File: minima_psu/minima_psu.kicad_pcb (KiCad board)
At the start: 2 copper layers, 78 x 90 mm, 26 parts, among them J1 Screw_Terminal_01x03, J2 Screw_Terminal_01x02, J3 Screw_Terminal_01x03, J4 Screw_Terminal_01x03, J5 Screw_Terminal_01x03, J6 Screw_Terminal_01x03

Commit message: Minor PCB adjustements
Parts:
- moved C4 15.4 mm to (104.2, 126.8), turned to 270 degrees
- moved C6 13.8 mm to (138.2, 141.8)
- moved C7 10.9 mm to (126.2, 126.8)
- moved J2 9.00 mm to (136.2, 151.8)
- moved J4 9.00 mm to (148.2, 151.8)
- moved J5 2.83 mm to (158.2, 75.8)
- moved R4 2.54 mm to (101.6, 116.8)
- moved J1 2.24 mm to (120.2, 75.8)
- moved J6 2.24 mm to (142.2, 75.8)
- moved D1 2.00 mm to (148.2, 141.8)
- moved C2 1.27 mm to (101.6, 97.8)
- moved C3 1.27 mm to (111.8, 97.8)
- moved R3 1.27 mm to (101.6, 105.4)
- moved R5 1.27 mm to (101.6, 113.0)
- moved C9 1.21 mm to (153.7, 97.8)
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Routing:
- net /ac_l: track 0.00 -> 102.3 mm
- net Earth_Protective: track 0.00 -> 65.7 mm
- net /ac_n: track 0.00 -> 39.6 mm
- net Net-(C6-Pad1): track 0.00 -> 38.6 mm
- net Net-(C2-Pad1): track 0.00 -> 17.5 mm
- net Net-(C3-Pad2): track 0.00 -> 13.2 mm
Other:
- net class ac_p added: clearance 2, trace_width 2.54, via_dia 0.8, via_drill 0.4
- net class ac_prot added: clearance 2, trace_width 5.08, via_dia 0.8, via_drill 0.4
- net class dc_p added: clearance 1, trace_width 5.08, via_dia 0.8, via_drill 0.4

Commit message: WIP: Layout of PCB.
Signed-off-by: Nenad Radulovic <nenad.b.radulovic@gmail.com>
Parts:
- added LOGO1: Kicad_Logo, Symbol:KiCad-Logo_5mm_Copper, F.Cu at (145.2, 86.8)
- added LOGO2: Kicad_Logo, Symbol:OSHW-Logo2_7.3x6mm_SilkScreen, F.Cu at (168.2, 84.8)
- moved C2 14.9 mm to (114.2, 89.8), turned to 180 degrees
- moved R2 13.2 mm to (106.2, 96.8)
- moved D2 11.3 mm to (100.2, 98.8), turned to 270 degrees
- moved R4 11.0 mm to (106.2, 106.8)
- moved C3 10.3 mm to (105.2, 89.8), turned to 180 degrees
- moved R3 5.86 mm to (106.2, 101.8)
- moved R5 4.80 mm to (106.2, 111.8)
- moved C8 2.06 mm to (127.0, 99.8)
- moved C9 2.06 mm to (153.7, 99.8)
- moved J1 2.00 mm to (120.2, 77.8)
- moved J5 2.00 mm to (158.2, 77.8)
- moved J6 2.00 mm to (142.2, 77.8)
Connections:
- net Net-(C2-Pad1) renamed /acs_p
- net Net-(C3-Pad2) renamed /acs_n
- R3 pad 1: GNDPWR -> Net-(C3-Pad1)
- R3 pad 2: Net-(C3-Pad1) -> GNDPWR
- R5 pad 1: GNDPWR -> /vee
- R5 pad 2: /vee -> GNDPWR
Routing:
- net /acs_p: track 17.5 -> 0.00 mm
- net Net-(C3-Pad1): track 0.00 -> 14.1 mm
- net /acs_n: track 13.2 -> 0.00 mm
- net Net-(C2-Pad2): track 0.00 -> 8.24 mm
- added copper zone on B.Cu, net /acs_n
- added copper zone on B.Cu, net /acs_p

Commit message: WIP: Component routing & placement
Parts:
- removed the J4 at (148.2, 151.8)
- added C3: 100n, Capacitor_THT:C_Rect_L7.0mm_W3.5mm_P5.00mm, F.Cu at (130.8, 85.7)
- added C4: 100n, Capacitor_THT:C_Rect_L7.0mm_W3.5mm_P5.00mm, F.Cu at (148.0, 85.7)
- added C7: 100n, Capacitor_THT:C_Rect_L7.0mm_W3.5mm_P5.00mm, F.Cu at (156.8, 85.7)
- added C8: 100n, Capacitor_THT:C_Rect_L7.0mm_W3.5mm_P5.00mm, F.Cu at (139.1, 85.7)
- added J2: psupply, Connector_Phoenix_MC:PhoenixContact_MCV_1,5_3-G-3.81_1x03_P3.81mm_Vertical, F.Cu at (158.2, 77.8)
- J1: value Screw_Terminal_01x03 -> power; footprint TerminalBlock_Phoenix:TerminalBlock_Phoenix_MKDS-3-3-5.08_1x03_P5.08mm_Horizontal -> Connector_Phoenix_MC:PhoenixContact_MCV_1,5_3-G-3.81_1x03_P3.81mm_Vertical
- J3: value Screw_Terminal_01x03 -> psupply; footprint TerminalBlock_Phoenix:TerminalBlock_Phoenix_MKDS-3-3-5.08_1x03_P5.08mm_Horizontal -> Connector_Phoenix_MC:PhoenixContact_MCV_1,5_3-G-3.81_1x03_P3.81mm_Vertical
- J4: renamed from J2; value Screw_Terminal_01x02 -> switch
- J5: value Screw_Terminal_01x03 -> ac_in
- J6: value Screw_Terminal_01x03 -> transformer
- moved J5 88.2 mm to (110.2, 151.8), turned to 0 degrees
- moved J3 80.6 mm to (142.2, 77.8), turned to 180 degrees
- moved J6 74.2 mm to (148.2, 151.8), turned to 0 degrees
- moved LOGO1 20.2 mm to (127.0, 78.1), turned to 270 degrees
- moved C6 1.86 mm to (154.3, 101.6)
- moved C2 1.75 mm to (127.0, 101.6)
- renumbered C2 to C1, C4 to C10, C7 to C11, C5 to C12, C1 to C13, C8 to C2, C3 to C5, C9 to C6, C6 to C9, D2 to D1, D1 to D2, MH3 to MH2, MH2 to MH3, R2 to R1, R3 to R2, R4 to R3, R5 to R4, R1 to R5
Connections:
- C11 pad 2: Net-(C6-Pad1) -> Net-(C11-Pad2)
- C9 pad 1: Net-(C6-Pad1) -> Net-(C11-Pad2)
- J3 pad 1: /ac_l -> /vcc
- J3 pad 2: Earth_Protective -> GNDPWR
- J3 pad 3: /ac_n -> /vee
- J4 pad 1: Net-(C6-Pad1) -> /ac_l
- J4 pad 2: /ac_l -> Net-(C11-Pad2)
- J5 pad 1: /vcc -> /ac_l
- J5 pad 2: GNDPWR -> Earth_Protective
- J5 pad 3: /vee -> /ac_n
- J6 pad 1: /vcc -> Net-(C11-Pad2)
- J6 pad 2: GNDPWR -> Earth_Protective
- J6 pad 3: /vee -> /ac_n
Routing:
- net Earth_Protective: track 65.7 -> 111.0 mm
- net /ac_n: track 39.6 -> 83.2 mm
- net Net-(C6-Pad1): track 39.1 -> 0.00 mm
- net Net-(C11-Pad2): track 0.00 -> 30.2 mm
- net GNDPWR: track 0.00 -> 20.8 mm
- net /ac_l: track 102.3 -> 102.8 mm
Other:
- net class ac_prot: trace_width 5.08 -> 2.54
- net class dc_p: trace_width 5.08 -> 2.54

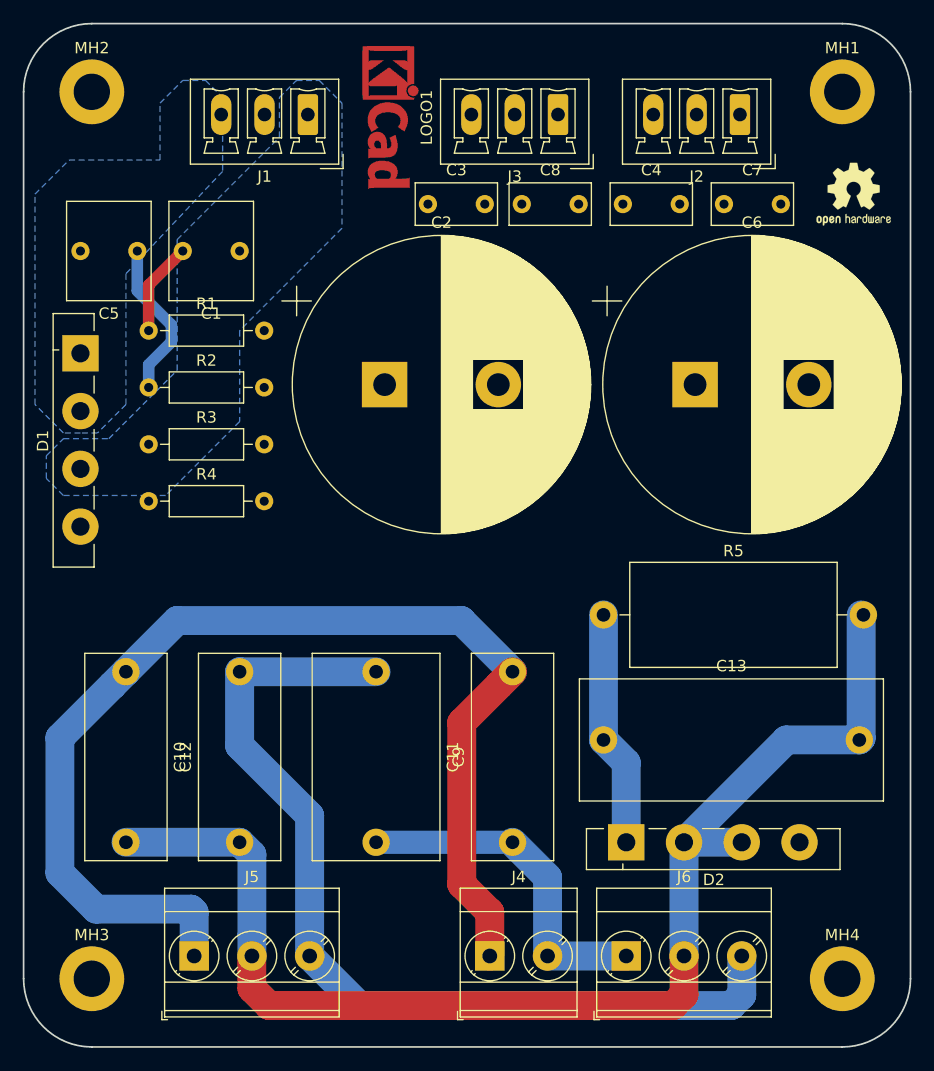
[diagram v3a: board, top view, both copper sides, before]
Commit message: Added comment about matching connector
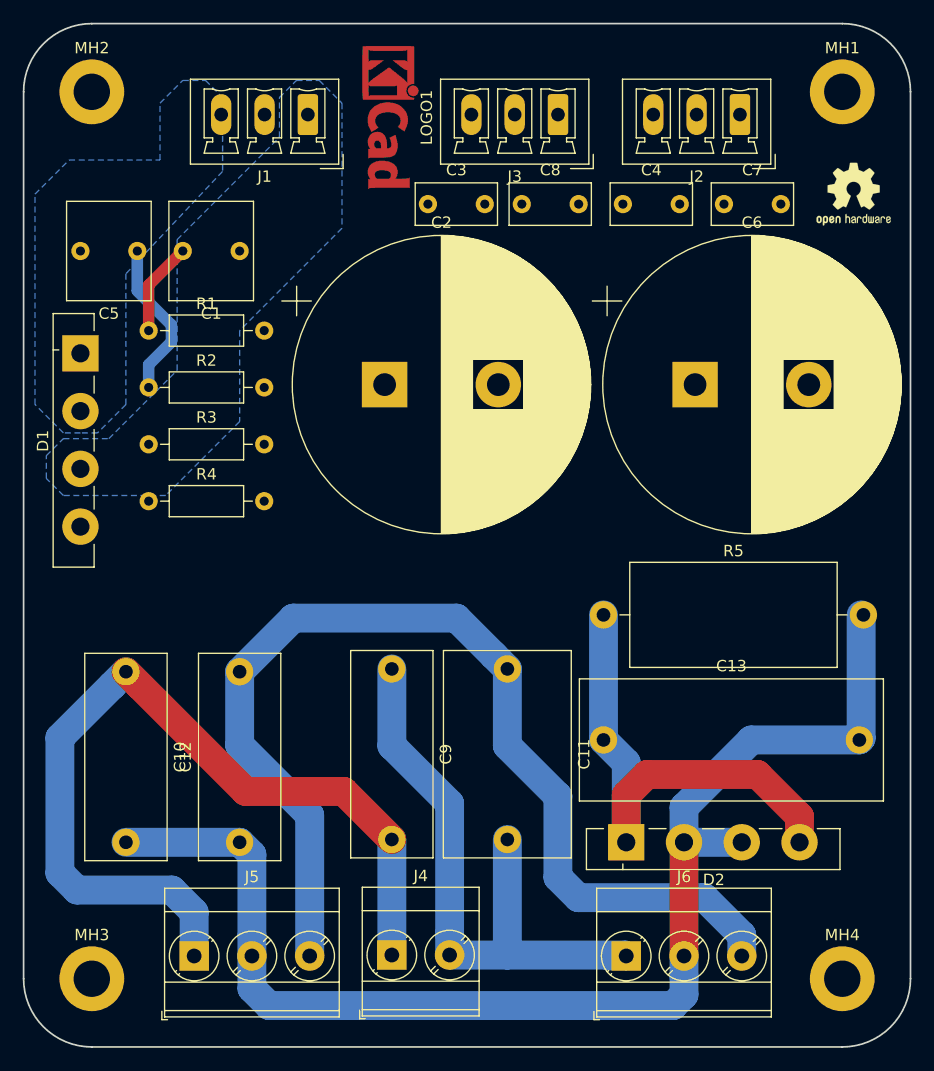
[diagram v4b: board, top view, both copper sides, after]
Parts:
- moved C9 18.6 mm to (127.6, 126.6), turned to 270 degrees
- moved C11 11.5 mm to (137.8, 126.6)
- moved J4 8.62 mm to (127.6, 151.8)
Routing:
- net /ac_l: track 102.8 -> 76.8 mm
- net Net-(C11-Pad2): track 30.2 -> 54.5 mm
- net GNDPWR: track 20.8 -> 44.8 mm
- net /ac_n: track 83.2 -> 95.2 mm
- net Earth_Protective: track 111.0 -> 112.8 mm
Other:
- net class ac_p: clearance 2 -> 1
- net class ac_prot: clearance 2 -> 1
